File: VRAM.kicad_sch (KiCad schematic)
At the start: 4 parts, among them U801 IDT7134, U802 IDT7134, U803 GAL22V10, U804 74ACT574

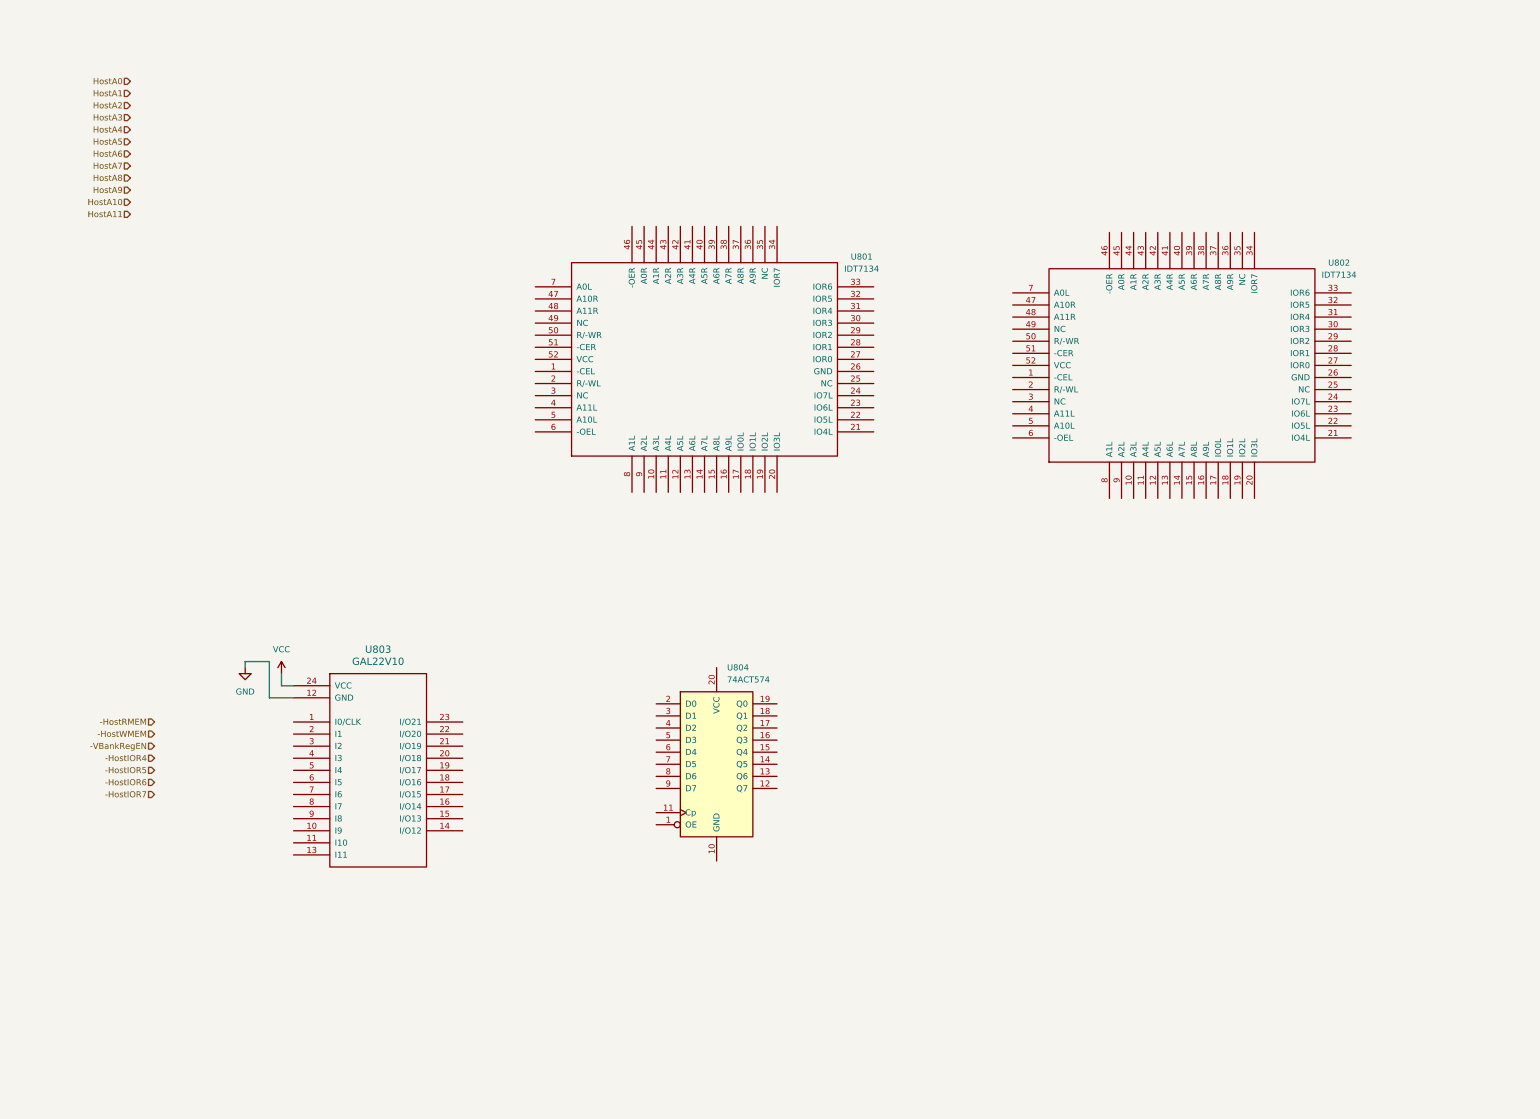
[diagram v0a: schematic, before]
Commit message: more work on VRAM host interfacing
Fixed error in IDT7134 symbol.

Working on address decoding and lower/upper VRAM
selection. Since we're using a GAL to decode the host
control signals, it can just do its own logic to
recognize when the upper part of the I/O region
is being accessed. The CPU/glue logic module generates
-IOR4..-IOR7 signals when this region is accessed,
but they're not present on the bus. However, the
control signal decoding GAL can just look at
A8..A15 to figure out when the VRAM is being
accessed.
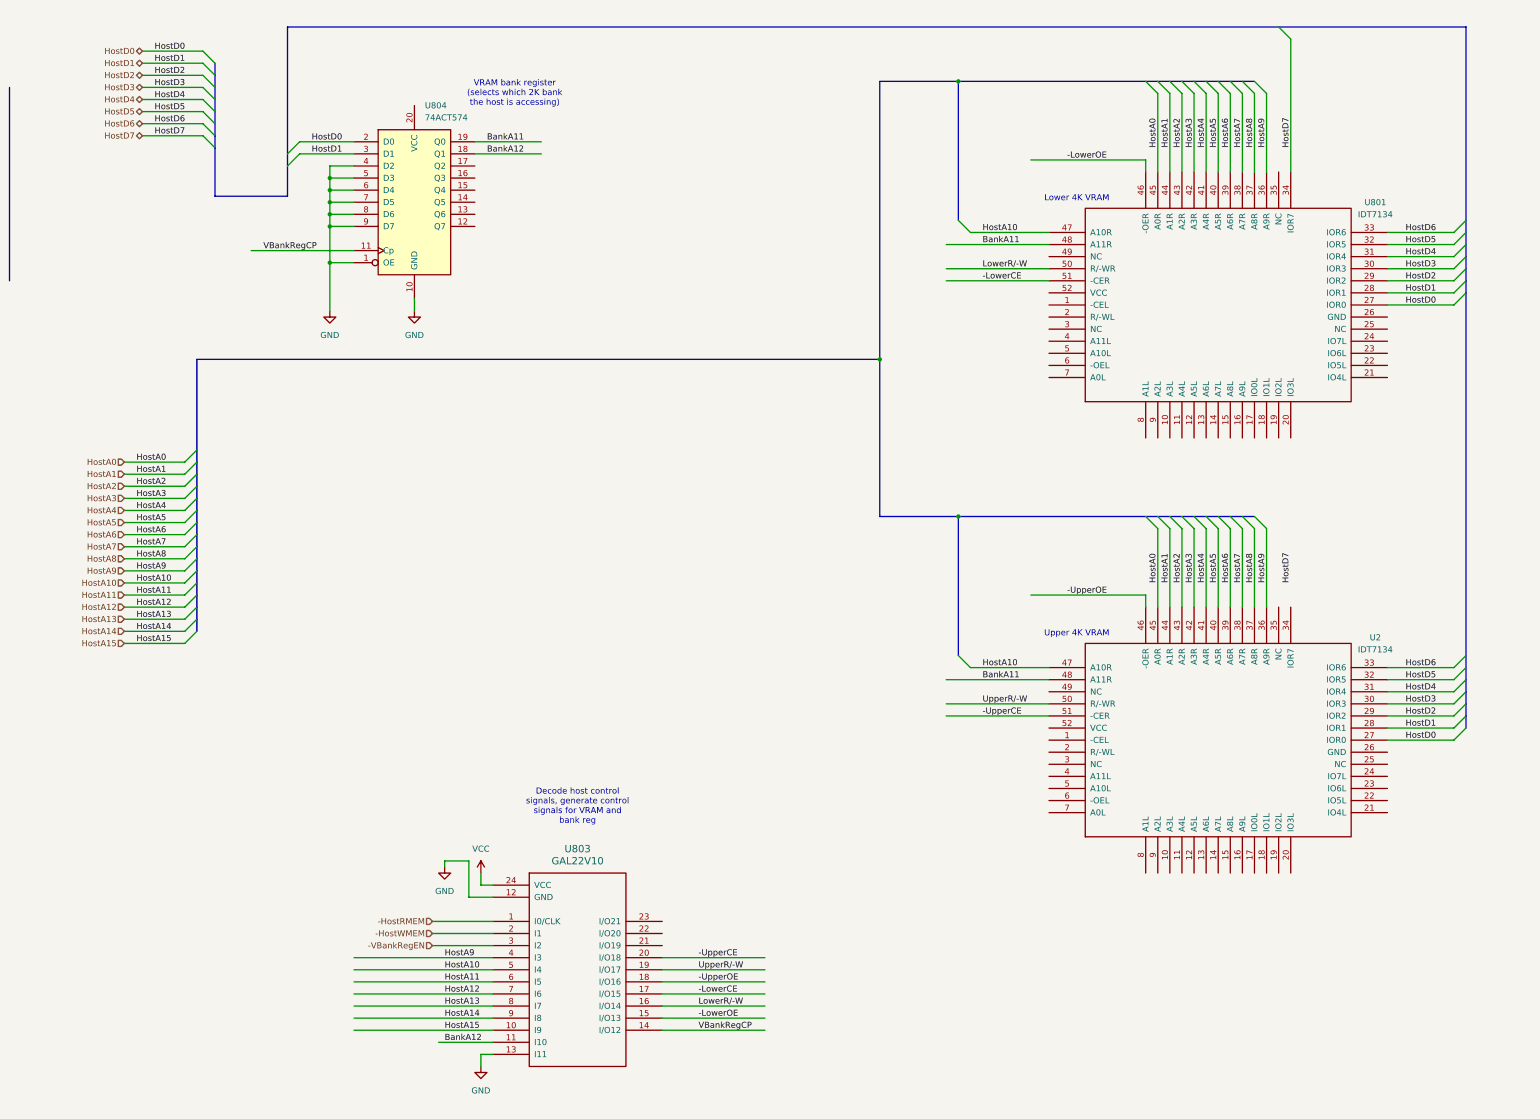
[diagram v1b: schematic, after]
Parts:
- removed U802: IDT7134, MODULE, symbol IDT7134:IDT7134
- added U2: IDT7134, MODULE, symbol IDT7134:IDT7134
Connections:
- net -HostRMEM: now also U803.1 (I0/CLK)
- net -HostWMEM: now also U803.2 (I1)
- net -VBankRegEN: now also U803.3 (I2)
- net GND: now also U803.13 (I11), U804.1 (OE), U804.10 (GND), U804.4 (D2), U804.5 (D3), U804.6 (D4), U804.7 (D5), U804.8 (D6), U804.9 (D7)
- net HostA0: now also U801.45 (A0R), U2.45 (A0R)
- net HostA1: now also U801.44 (A1R), U2.44 (A1R)
- net HostA10: now also U801.47 (A10R), U803.5 (I4), U2.47 (A10R)
- net HostA11: now also U803.6 (I5)
- net HostA2: now also U801.43 (A2R), U2.43 (A2R)
- net HostA3: now also U801.42 (A3R), U2.42 (A3R)
- net HostA4: now also U801.41 (A4R), U2.41 (A4R)
- net HostA5: now also U801.40 (A5R), U2.40 (A5R)
- net HostA6: now also U801.39 (A6R), U2.39 (A6R)
- net HostA7: now also U801.38 (A7R), U2.38 (A7R)
- net HostA8: now also U801.37 (A8R), U2.37 (A8R)
- net HostA9: now also U801.36 (A9R), U803.4 (I3), U2.36 (A9R)
- net VBankRegCP: now reaches U804.11 (Cp)
- net VBankRegCP: now also U803.14 (I/O12)
- net BankA12: now reaches U804.18 (Q1)
- net BankA12: now also U803.11 (I10)
- net BankA11: now reaches U804.19 (Q0)
- net BankA11: now also U801.48 (A11R), U2.48 (A11R)
- net HostD0: now reaches U804.2 (D0)
- net HostD0: now also U801.27 (IOR0), U2.27 (IOR0)
- net HostD1: now reaches U804.3 (D1)
- net HostD1: now also U801.28 (IOR1), U2.28 (IOR1)
- net HostA15: now reaches U803.10 (I9)
- net -LowerOE: now reaches U803.15 (I/O13)
- net -LowerOE: now also U801.46 (-OER)
- net LowerR/-W: now reaches U803.16 (I/O14)
- net LowerR/-W: now also U801.50 (R/-WR)
- net -LowerCE: now reaches U803.17 (I/O15)
- net -LowerCE: now also U801.51 (-CER)
- net -UpperOE: now reaches U803.18 (I/O16)
- net -UpperOE: now also U2.46 (-OER)
- net UpperR/-W: now reaches U803.19 (I/O17)
- net UpperR/-W: now also U2.50 (R/-WR)
- net -UpperCE: now reaches U803.20 (I/O18)
- net -UpperCE: now also U2.51 (-CER)
- net HostA12: now reaches U803.7 (I6)
- net HostA13: now reaches U803.8 (I7)
- net HostA14: now reaches U803.9 (I8)
- net HostD2: now reaches U801.29 (IOR2)
- net HostD2: now also U2.29 (IOR2)
- net HostD3: now reaches U801.30 (IOR3)
- net HostD3: now also U2.30 (IOR3)
- net HostD4: now reaches U801.31 (IOR4)
- net HostD4: now also U2.31 (IOR4)
- net HostD5: now reaches U801.32 (IOR5)
- net HostD5: now also U2.32 (IOR5)
- net HostD6: now reaches U801.33 (IOR6)
- net HostD6: now also U2.33 (IOR6)
- net HostD7: now reaches U801.34 (IOR7)
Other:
- note added: "Decode host control signals, generate control signals for VRAM and bank reg"
- note added: "Lower 4K VRAM"
- note added: "Upper 4K VRAM"
- note added: "VRAM bank register (selects which 2K bank the host is accessing)"
- moved on the sheet: U803, U804

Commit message: relative complete VRAM module design?
Added the interface to the display controller memory
fetch hardware (is basically just address signals and
data output.) The readout A12 signal is used to select
the VRAM device to read from (low or high). The GAL
inverts this signal for reading from the high VRAM.
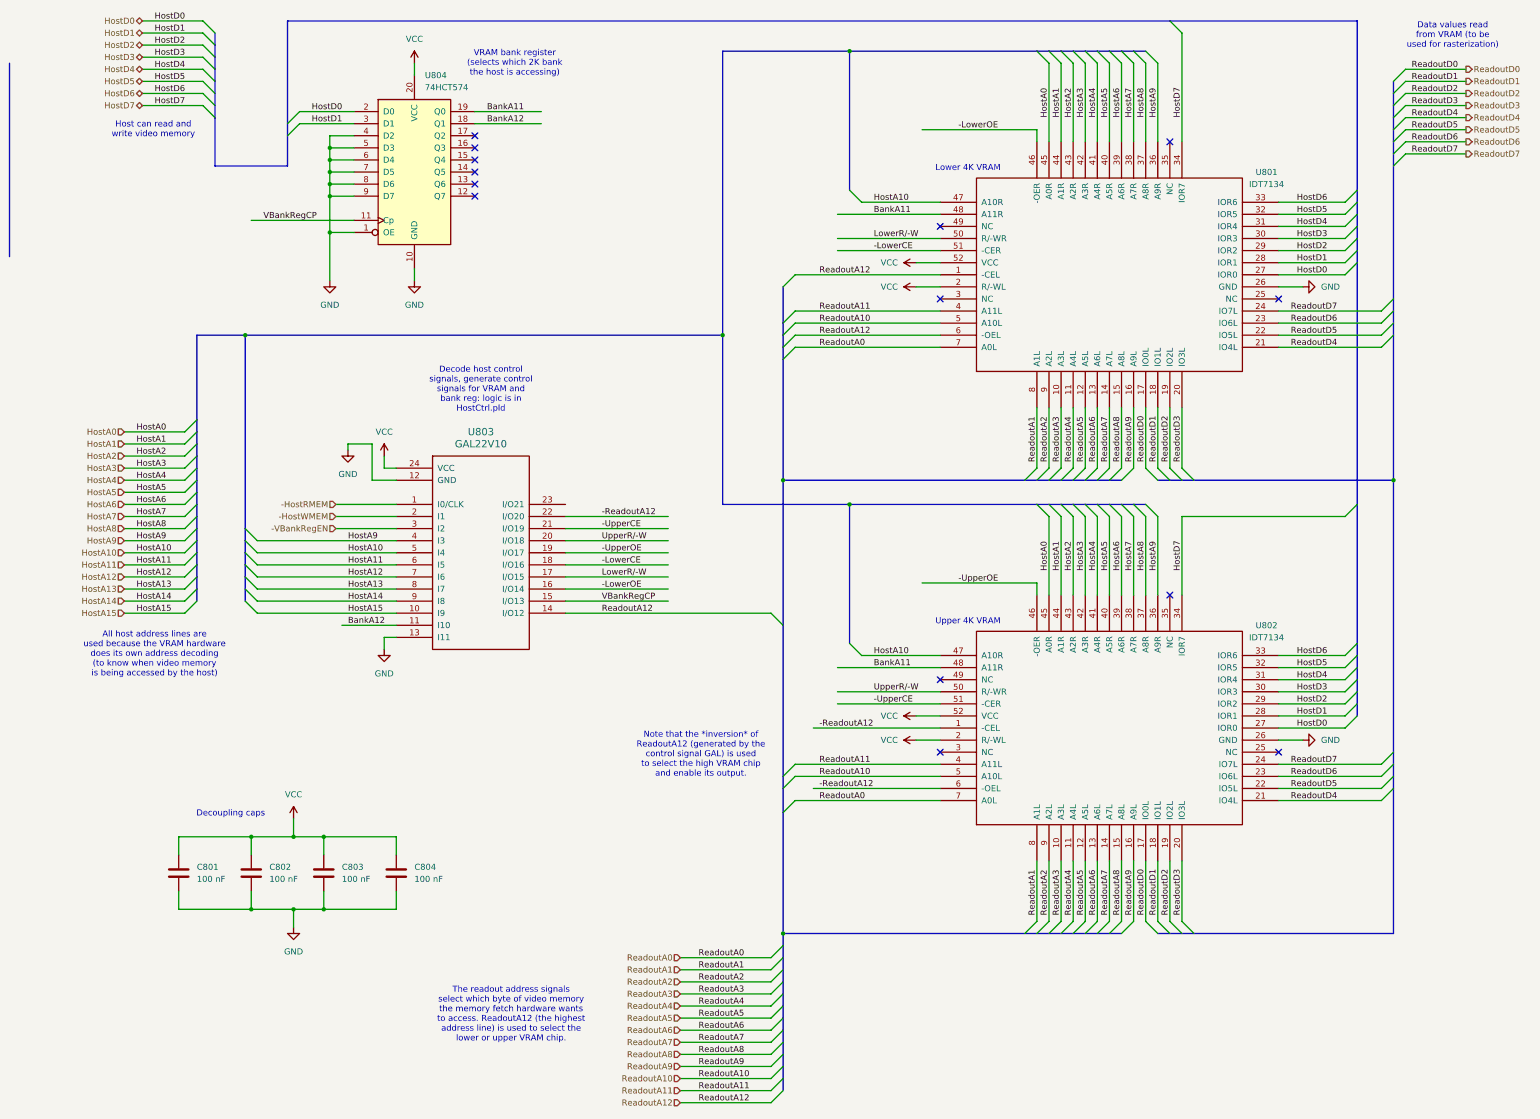
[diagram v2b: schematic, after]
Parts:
- added C801, C802, C803, C804: 100 nF, symbol Device:C
- U804: value 74ACT574 -> 74HCT574
- renumbered U2 to U802
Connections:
- net -LowerCE: now also U803.18 (I/O16); no longer U803.17 (I/O15)
- net -LowerOE: now also U803.16 (I/O14); no longer U803.15 (I/O13)
- net -UpperCE: now also U803.21 (I/O19); no longer U803.20 (I/O18)
- net -UpperOE: now also U803.19 (I/O17); no longer U803.18 (I/O16)
- net GND: now also U801.26 (GND), U802.26 (GND), C801.2, C802.2, C803.2, C804.2
- net HostD7: now also U802.34 (IOR7)
- net LowerR/-W: now also U803.17 (I/O15); no longer U803.16 (I/O14)
- net UpperR/-W: now also U803.20 (I/O18); no longer U803.19 (I/O17)
- net VBankRegCP: now also U803.15 (I/O13); no longer U803.14 (I/O12)
- net VCC: now also U801.2 (R/-WL), U801.52 (VCC), U802.2 (R/-WL), U802.52 (VCC), U804.20 (VCC), C801.1, C802.1, C803.1, C804.1
- net -ReadoutA12: now reaches U802.1 (-CEL)
- net -ReadoutA12: now also U802.6 (-OEL), U803.22 (I/O20)
- net ReadoutA3: now reaches U802.10 (A3L)
- net ReadoutA3: now also U801.10 (A3L)
- net ReadoutA4: now reaches U802.11 (A4L)
- net ReadoutA4: now also U801.11 (A4L)
- net ReadoutA5: now reaches U802.12 (A5L)
- net ReadoutA5: now also U801.12 (A5L)
- net ReadoutA6: now reaches U802.13 (A6L)
- net ReadoutA6: now also U801.13 (A6L)
- net ReadoutA7: now reaches U802.14 (A7L)
- net ReadoutA7: now also U801.14 (A7L)
- net ReadoutA8: now reaches U802.15 (A8L)
- net ReadoutA8: now also U801.15 (A8L)
- net ReadoutA9: now reaches U802.16 (A9L)
- net ReadoutA9: now also U801.16 (A9L)
- net ReadoutD0: now reaches U802.17 (IO0L)
- net ReadoutD0: now also U801.17 (IO0L)
- net ReadoutD1: now reaches U802.18 (IO1L)
- net ReadoutD1: now also U801.18 (IO1L)
- net ReadoutD2: now reaches U802.19 (IO2L)
- net ReadoutD2: now also U801.19 (IO2L)
- net ReadoutD3: now reaches U802.20 (IO3L)
- net ReadoutD3: now also U801.20 (IO3L)
- net ReadoutD4: now reaches U802.21 (IO4L)
- net ReadoutD4: now also U801.21 (IO4L)
- net ReadoutD5: now reaches U802.22 (IO5L)
- net ReadoutD5: now also U801.22 (IO5L)
- net ReadoutD6: now reaches U802.23 (IO6L)
- net ReadoutD6: now also U801.23 (IO6L)
- net ReadoutD7: now reaches U802.24 (IO7L)
- net ReadoutD7: now also U801.24 (IO7L)
- net ReadoutA11: now reaches U802.4 (A11L)
- net ReadoutA11: now also U801.4 (A11L)
- net ReadoutA10: now reaches U802.5 (A10L)
- net ReadoutA10: now also U801.5 (A10L)
- net ReadoutA0: now reaches U802.7 (A0L)
- net ReadoutA0: now also U801.7 (A0L)
- net ReadoutA1: now reaches U802.8 (A1L)
- net ReadoutA1: now also U801.8 (A1L)
- net ReadoutA2: now reaches U802.9 (A2L)
- net ReadoutA2: now also U801.9 (A2L)
- net ReadoutA12: now reaches U801.1 (-CEL)
- net ReadoutA12: now also U801.6 (-OEL), U803.14 (I/O12)
- no-connect marks 0 -> 14
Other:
- note added: "All host address lines are used because the VRAM hardware does its own address decoding (to know when video memory is being accessed by the host)"
- note added: "Data values read from VRAM (to be used for rasterization)"
- note added: "Decode host control signals, generate control signals for VRAM and bank reg: logic is in HostCtrl.pld"
- note added: "Decoupling caps"
- note added: "Host can read and write video memory"
- note added: "Note that the *inversion* of ReadoutA12 (generated by the control signal GAL) is used to select the high VRAM chip and enable its output."
- note added: "The readout address signals select which byte of video memory the memory fetch hardware wants to access. ReadoutA12 (the highest address line) is used to select the lower or upper VRAM chip."
- note removed: "Decode host control signals, generate control signals for VRAM and bank reg"
- moved on the sheet: U801, U802, U803, U804
